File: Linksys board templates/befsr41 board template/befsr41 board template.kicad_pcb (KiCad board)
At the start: 2 copper layers, 160 x 138 mm, 46 parts, among them J1 RJ45, J2 RJ45, J3 RJ45, J4 RJ45, J5 RJ45, J6 Barrel_Jack_Switch, J7 switched ground, J8 RJ45, SW2 reset, U1 AMS1117-3.3, U2 AMS1117-5.0, U3 YAAJ_DCDC_StepDown_LM2596

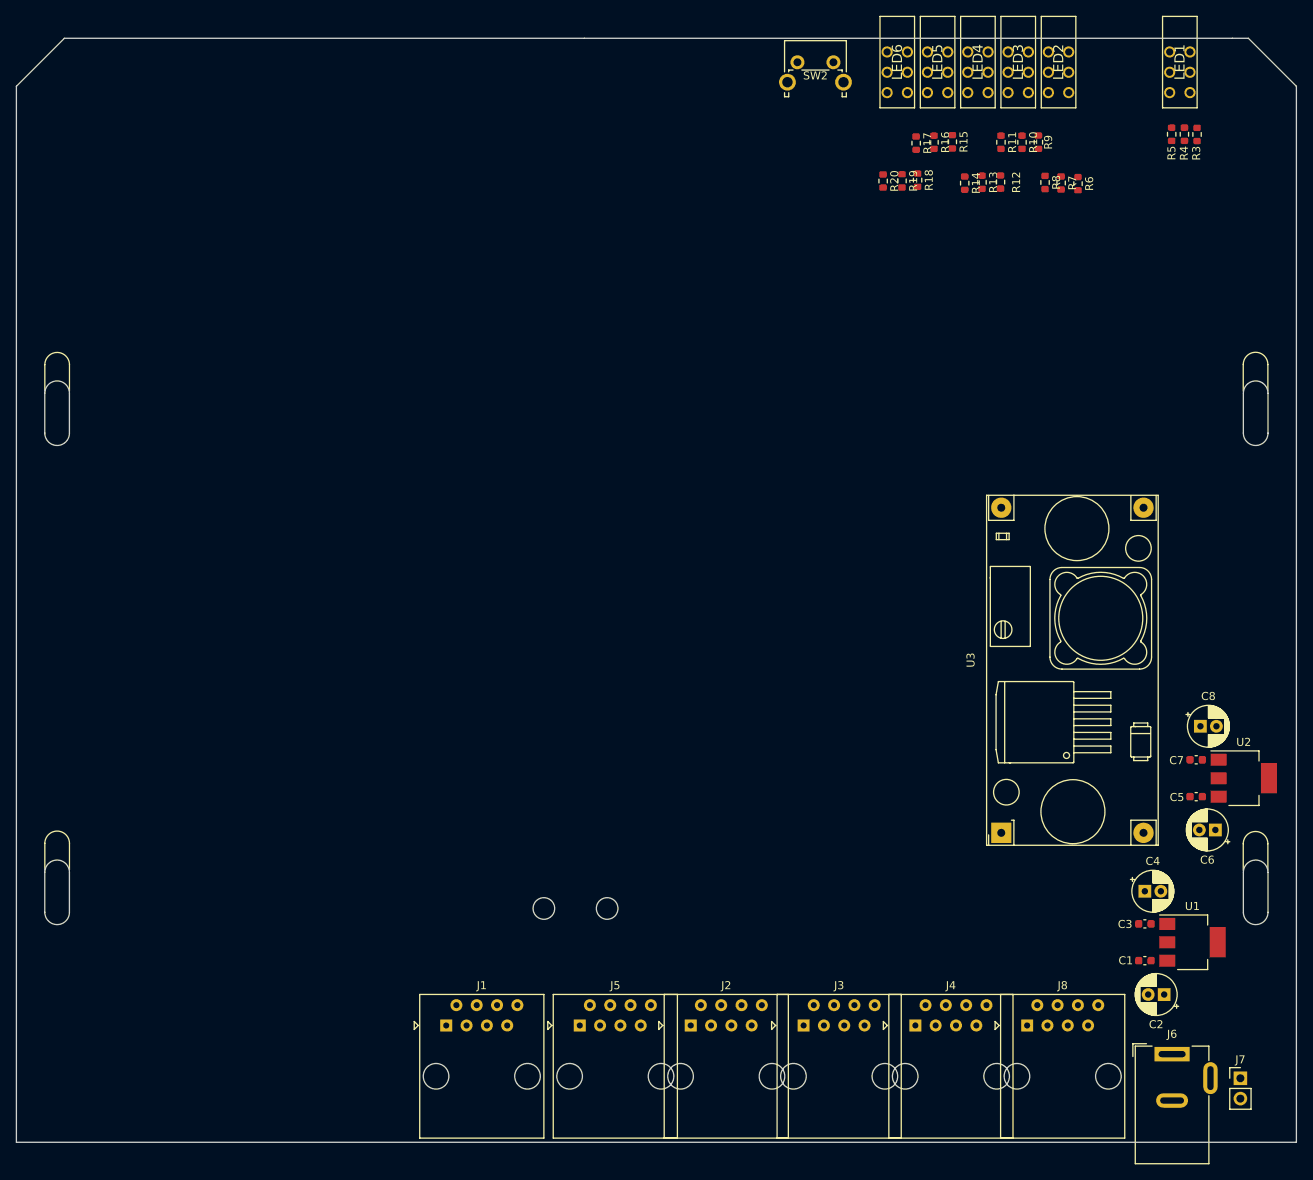
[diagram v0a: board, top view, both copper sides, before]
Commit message: tweaks to locations based on 1:1 printouts
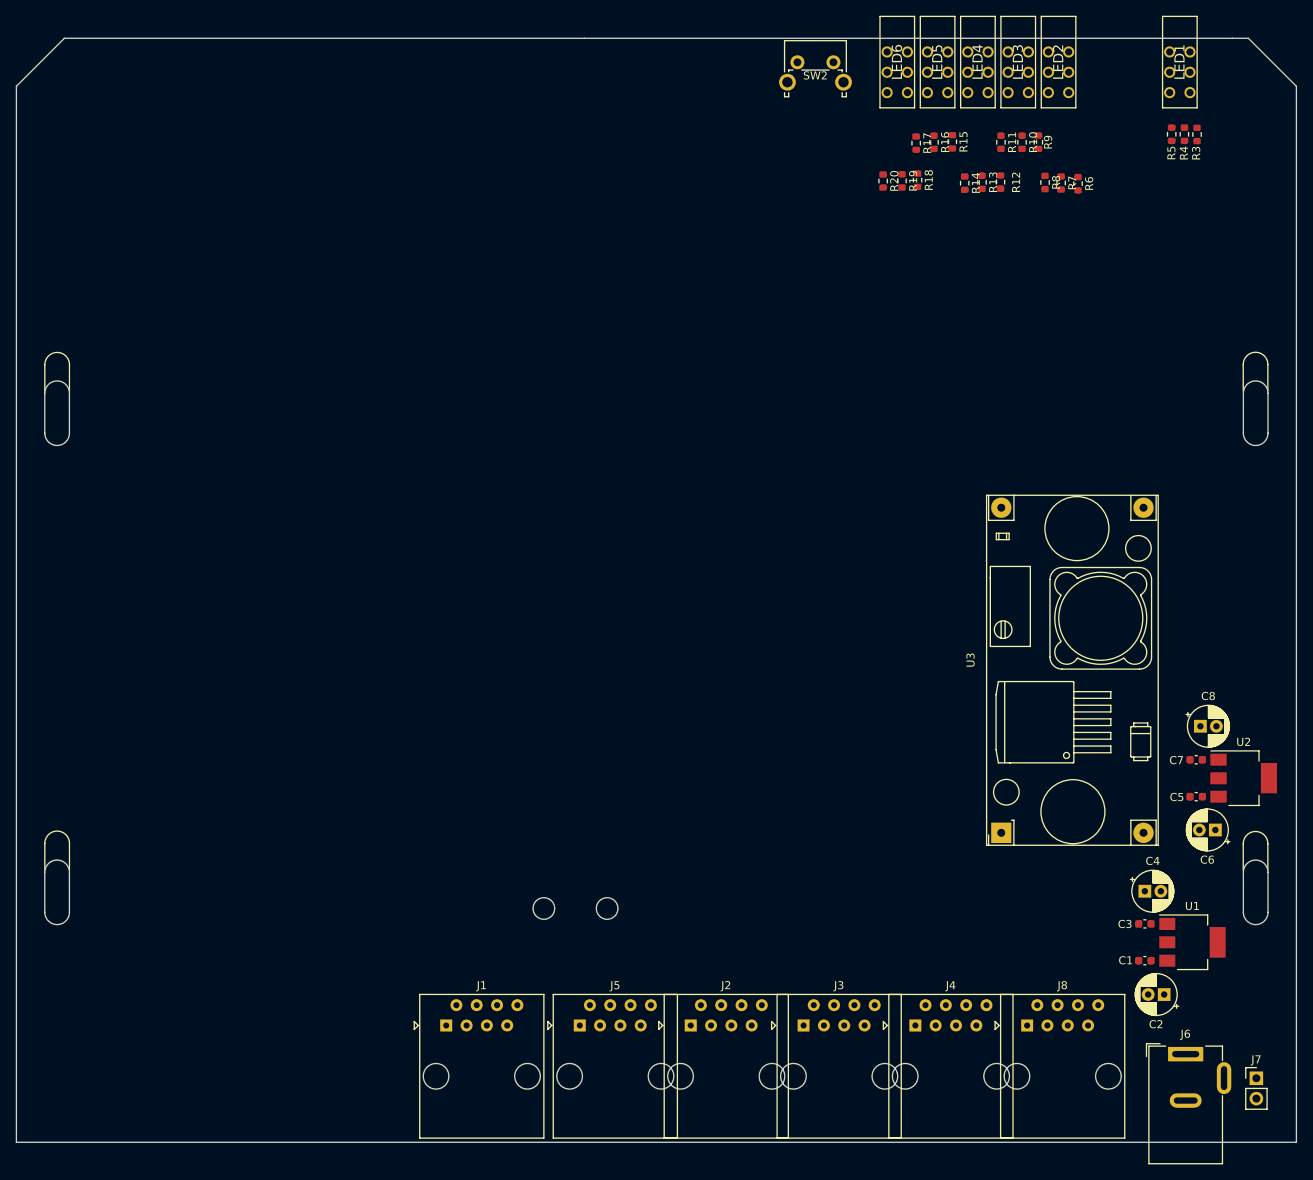
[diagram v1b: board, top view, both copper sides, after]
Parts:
- moved J7 2.00 mm to (222.0, 152.0)
- moved J6 1.70 mm to (213.2, 149.0)
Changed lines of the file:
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@@
   )
   (footprint "Connector_PinHeader_2.54mm:PinHeader_1x02_P2.54mm_Vertical" (layer "F.Cu")
-    (at 220 152)
+    (at 222 152)
     (descr "Through hole straight pin header, 1x02, 2.54mm pitch, single row")
     (tags "Through hole pin header THT 1x02 2.54mm single row")
@@
   )
   (footprint "Connector_BarrelJack:BarrelJack_Wuerth_6941xx301002" (layer "F.Cu")
-    (at 211.46 148.98)
+    (at 213.16 148.98)
     (descr "Wuerth electronics barrel jack connector (5.5mm outher diameter, inner diameter 2.05mm or 2.55mm depending on exact order number), See: http://katalog.we-online.de/em/datasheet/6941xx301002.pdf")
     (tags "connector barrel jack")
@@
   (gr_line (start 220.355001 66.1) (end 220.355001 62.779649) (layer "F.SilkS") (width 0.1))
   (gr_line (start 223.435034 126) (end 223.435034 122.689649) (layer "F.SilkS") (width 0.1))
-  (gr_arc (start 70.555001 62.8) (mid 72.1 61.270346) (end 73.635033 62.81) (layer "F.SilkS") (width 0.1))
+  (gr_arc (start 70.555001 62.8) (mid 72.1 61.270345) (end 73.635033 62.81) (layer "F.SilkS") (width 0.1))
   (gr_line (start 220.355002 126) (end 220.355002 122.679649) (layer "F.SilkS") (width 0.1))
   (gr_line (start 70.555001 66.120351) (end 70.555001 62.8) (layer "F.SilkS") (width 0.1))
-  (gr_arc (start 220.355001 62.779649) (mid 221.9 61.249996) (end 223.435033 62.789649) (layer "F.SilkS") (width 0.1))
+  (gr_arc (start 220.355001 62.779649) (mid 221.9 61.249995) (end 223.435033 62.789649) (layer "F.SilkS") (width 0.1))
   (gr_line (start 73.635033 125.950002) (end 73.635033 122.639651) (layer "F.SilkS") (width 0.1))
   (gr_line (start 73.635033 66.120351) (end 73.635033 62.81) (layer "F.SilkS") (width 0.1))
-  (gr_arc (start 220.355002 122.679649) (mid 221.900001 121.149997) (end 223.435034 122.689649) (layer "F.SilkS") (width 0.1))
+  (gr_arc (start 220.355002 122.679649) (mid 221.900001 121.149996) (end 223.435034 122.689649) (layer "F.SilkS") (width 0.1))
   (gr_line (start 223.435033 66.1) (end 223.435033 62.789649) (layer "F.SilkS") (width 0.1))
-  (gr_arc (start 70.555001 122.629651) (mid 72.1 121.099997) (end 73.635033 122.639651) (layer "F.SilkS") (width 0.1))
+  (gr_arc (start 70.555001 122.629651) (mid 72.1 121.099996) (end 73.635033 122.639651) (layer "F.SilkS") (width 0.1))
   (gr_line (start 70.555001 125.950002) (end 70.555001 122.629651) (layer "F.SilkS") (width 0.1))
   (gr_line (start 227.6 123.8) (end 222.4 123.7) (layer "Cmts.User") (width 0.15))
